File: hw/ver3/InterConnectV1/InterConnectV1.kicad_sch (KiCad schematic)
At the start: 3 parts, among them J1 Conn_02x04_Odd_Even, J3 RJ45, U5 SP3485EN

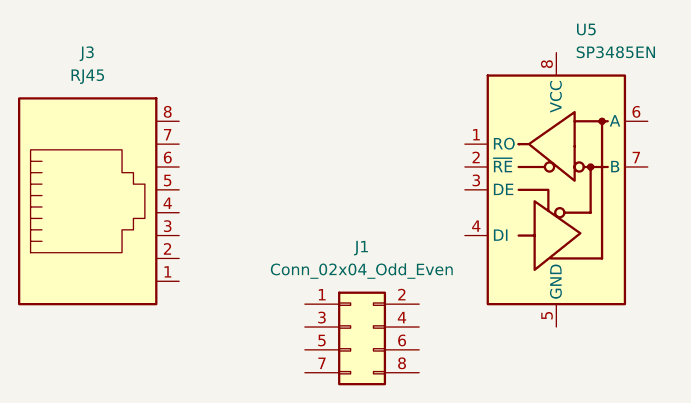
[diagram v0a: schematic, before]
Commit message: Redo some charger routing. Improve design for interconnect
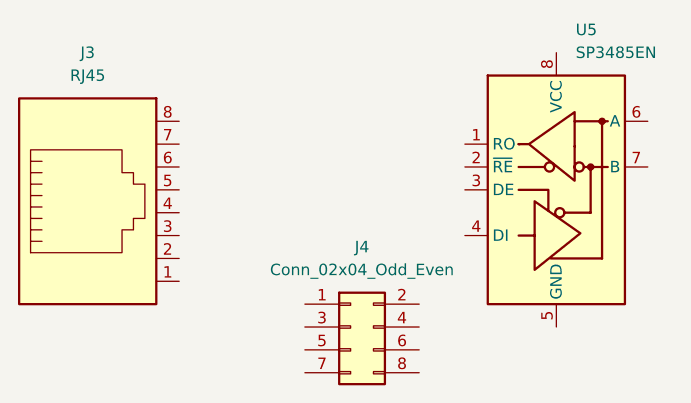
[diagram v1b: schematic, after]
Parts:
- renumbered J1 to J4
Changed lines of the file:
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@@
 		(dnp no)
 		(fields_autoplaced yes)
-		(property "Reference" "J1"
+		(property "Reference" "J4"
 			(at 125.73 93.98 0)
 			(effects
@@
 		)
 		(instances
+			(project "ChargerV3"
+				(path "/93408532-1ffa-463d-873c-16289d2b7987/f8cdf9d7-add1-4ff8-8430-918a71e3d1f9/aa801e4b-edfe-4a01-9e20-8e9249af9b44"
+					(reference "J4")
+					(unit 1)
+				)
+			)
 			(project ""
 				(path "/93a5de3b-2dc1-4e4f-9e25-5e90260a5115"
@@
 		)
 		(instances
+			(project "ChargerV3"
+				(path "/93408532-1ffa-463d-873c-16289d2b7987/f8cdf9d7-add1-4ff8-8430-918a71e3d1f9/aa801e4b-edfe-4a01-9e20-8e9249af9b44"
+					(reference "J3")
+					(unit 1)
+				)
+			)
 			(project "InterConnectV1"
 				(path "/93a5de3b-2dc1-4e4f-9e25-5e90260a5115"
@@
 		)
 		(instances
+			(project "ChargerV3"
+				(path "/93408532-1ffa-463d-873c-16289d2b7987/f8cdf9d7-add1-4ff8-8430-918a71e3d1f9/aa801e4b-edfe-4a01-9e20-8e9249af9b44"
+					(reference "U5")
+					(unit 1)
+				)
+			)
 			(project "InterConnectV1"
 				(path "/93a5de3b-2dc1-4e4f-9e25-5e90260a5115"

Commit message: Initial schematic for InterConnectV1
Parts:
- added C901, C905, C907: 10uF, Capacitor_SMD:C_0603_1608Metric, symbol Device:C
- added C902, C903, C904: 100nF, Capacitor_SMD:C_0603_1608Metric, symbol Device:C
- added C906, C908: 100uF-16v, Capacitor_SMD:CP_Elec_6.3x5.4, symbol Device:C_Polarized
- added D901: ACTIVITY, LED_SMD:LED_0805_2012Metric, symbol Device:LED
- added D902: PGOOD, LED_SMD:LED_0805_2012Metric, symbol Device:LED
- added D903: STPS360AF, Diode_SMD:D_SOD-128, symbol Device:D_Schottky
- added J902: TermEnable, Connector_PinHeader_2.54mm:PinHeader_1x02_P2.54mm_Vertical, symbol Connector:Conn_01x02_Pin
- added L901: 15uH, Inductor_SMD:L_12x12mm_H4.5mm, symbol Device:L_Ferrite
- added Q901: 2N7002, Package_TO_SOT_SMD:SOT-23, symbol Transistor_FET:2N7002
- added R901, R903: 47k, Resistor_SMD:R_0603_1608Metric, symbol Device:R_US
- added R902, R905, R906, R907, R908, R910: 10k, Resistor_SMD:R_0603_1608Metric, symbol Device:R_US
- added R904: 120, Resistor_SMD:R_0603_1608Metric, symbol Device:R_US
- added R909: 88.7k, Resistor_SMD:R_0603_1608Metric, symbol Device:R_US
- added U901: ST1S14PHR, Package_SO:TI_SO-PowerPAD-8, symbol Regulator_Switching:ST1S14PHR
- added U903: AMS1117-3.3, Package_TO_SOT_SMD:SOT-223-3_TabPin2, symbol Regulator_Linear:AMS1117-3.3
- added U904: AMS1117-5.0, Package_TO_SOT_SMD:SOT-223-3_TabPin2, symbol Regulator_Linear:AMS1117-5.0
- J901: renamed from J3; footprint (none) -> Connector_RJ:RJ45_Amphenol_54602-x08_Horizontal; Digikey (none) -> 609-1046-ND; LCSC (none) -> C2847314
- J903: renamed from J4; value Conn_02x04_Odd_Even -> DataBusSelector; Digikey (none) -> PH2-08-UA; LCSC (none) -> C492421
- U902: renamed from U5; Digikey (none) -> 4518-SP3485EENTR-ND; LCSC (none) -> C668205
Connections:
- net IO_DATA_A1: now reaches J903.1 (Pin_1)
- net IO_DATA_A1: now also J901.1
- net at J903.2 (Pin_2): now also J903.4 (Pin_4), U902.6 (A), J902.1 (Pin_1)
- net IO_DATA_A2: now reaches J903.3 (Pin_3)
- net IO_DATA_A2: now also J901.3
- net IO_DATA_B1: now reaches J903.5 (Pin_5)
- net IO_DATA_B1: now also J901.2
- net at J903.6 (Pin_6): now also J903.8 (Pin_8), U902.7 (B), R904.1
- net IO_DATA_B2: now reaches J903.7 (Pin_7)
- net IO_DATA_B2: now also J901.6
- net IO_PWR_+48V: now reaches J901.4
- net IO_PWR_+48V: now also J901.5, C901.1, C902.1, R901.1, R903.1, U901.5 (EN2), U901.7 (VIN)
- net GND: now reaches J901.7
- net GND: now also J901.8, U902.5 (GND), C901.2, C902.2, C904.2, C905.2, C906.2, C907.2, C908.2, D903.2 (A), Q901.2 (S), R902.1, R905.1, R906.1, R907.1, R908.1, R910.1, U901.3 (~{EN1}), U901.6 (GND), U901.9 (PADGND), U903.1 (GND), U904.1 (GND)
- net IC_DATA_OUT: now reaches U902.1 (RO)
- net IC_DATA_OUT: now also R907.2
- net IC_RTX_EN: now reaches U902.2 (~{RE})
- net IC_RTX_EN: now also U902.3 (DE), R906.2
- net IC_DATA_IN: now reaches U902.4 (DI)
- net IC_DATA_IN: now also R905.2
- net +3V3: now reaches U902.8 (VCC)
- net +3V3: now also C904.1
- new net: C903.1, D903.1 (K), L901.2, U901.8 (SW)
- new net: D901.2 (A), R901.2
- new net: D902.1 (K), U901.2 (PG)
- new net: D902.2 (A), R903.2
- new net: R908.2, R909.2, U901.4 (FB)
- new net: C903.2, U901.1 (BOOT)
- new net: J902.2 (Pin_2), R904.2
- new net: D901.1 (K), Q901.3 (D)
- new net IC_ACTIVITY_LED_DRIVE: Q901.1 (G), R902.2
- new net IC_PWR_12V: C906.1, C908.1, L901.1, R909.1, R910.2, U904.3 (VI)
- new net IC_PWR_3V3: C907.1, U903.2 (VO)
- new net IC_PWR_5V: C905.1, U903.3 (VI), U904.2 (VO)
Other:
- note added: "DC-DC Converter: 15V-48V IN, 12V 3A OUT"
- note added: "Data Activity LED Driver"
- note added: "Inductor P/N & pad sized to fit multiple components"
- note added: "Needs jumpers/shunts: - Digikey: QPC02SXGN-RC - LCSC: C100114"
- note added: "RJ45 IO Connector"
- note added: "RS485 Half-Duplex Transciever"
- moved on the sheet: J901, J903, U902

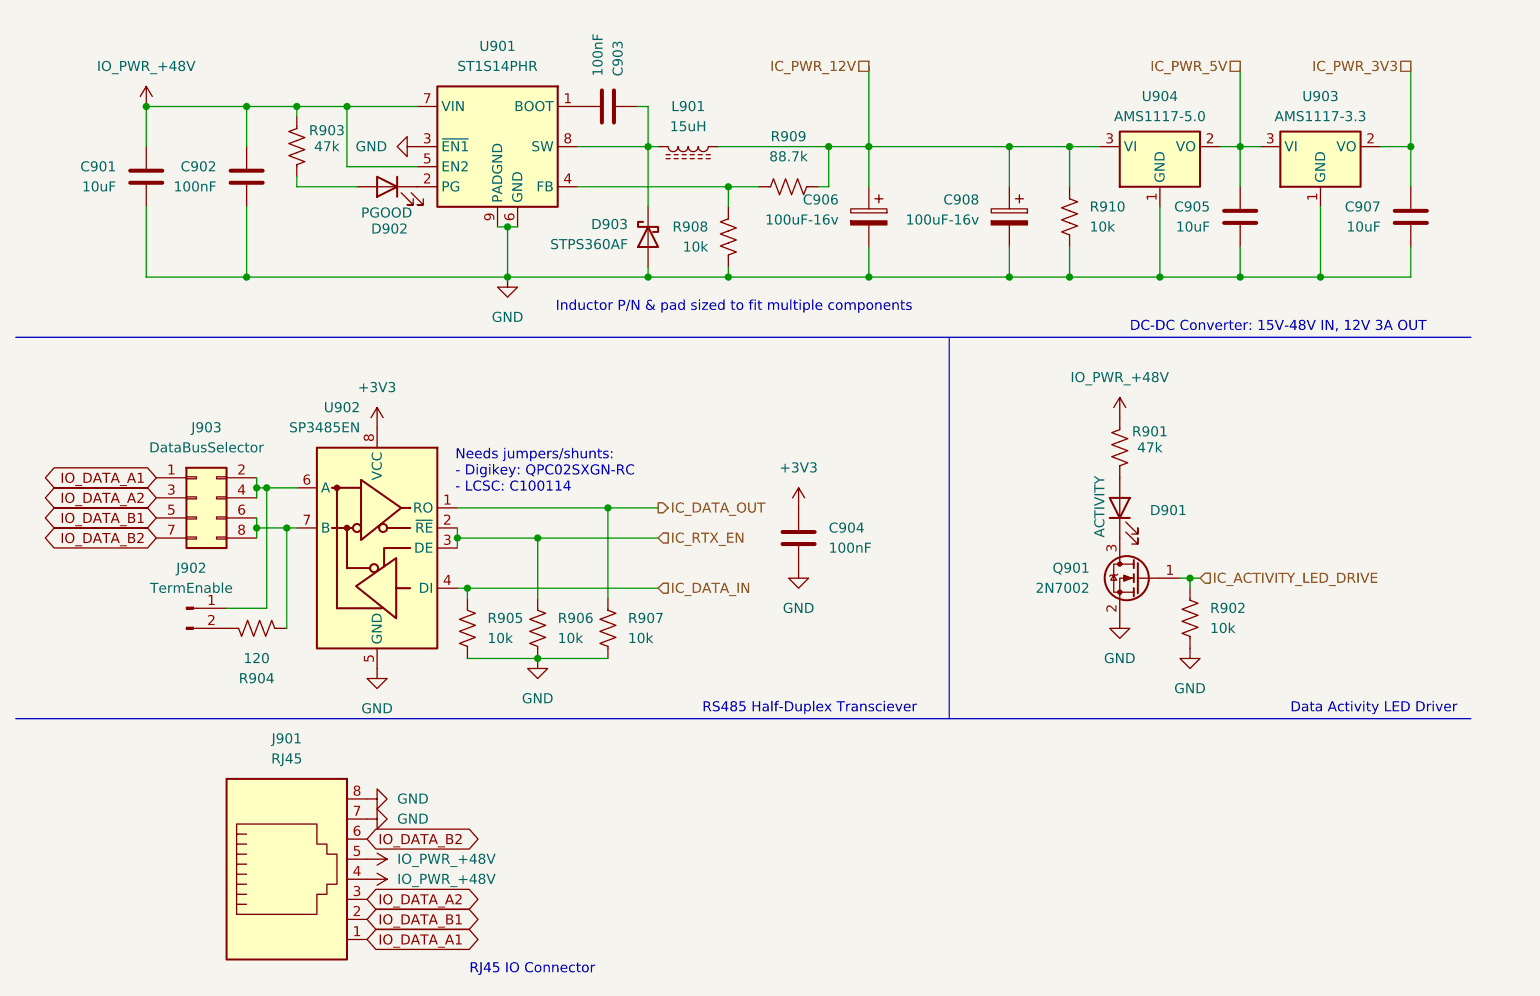
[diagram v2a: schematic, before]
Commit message: Nearly final charger schematic, updated with RS485 interconnect.
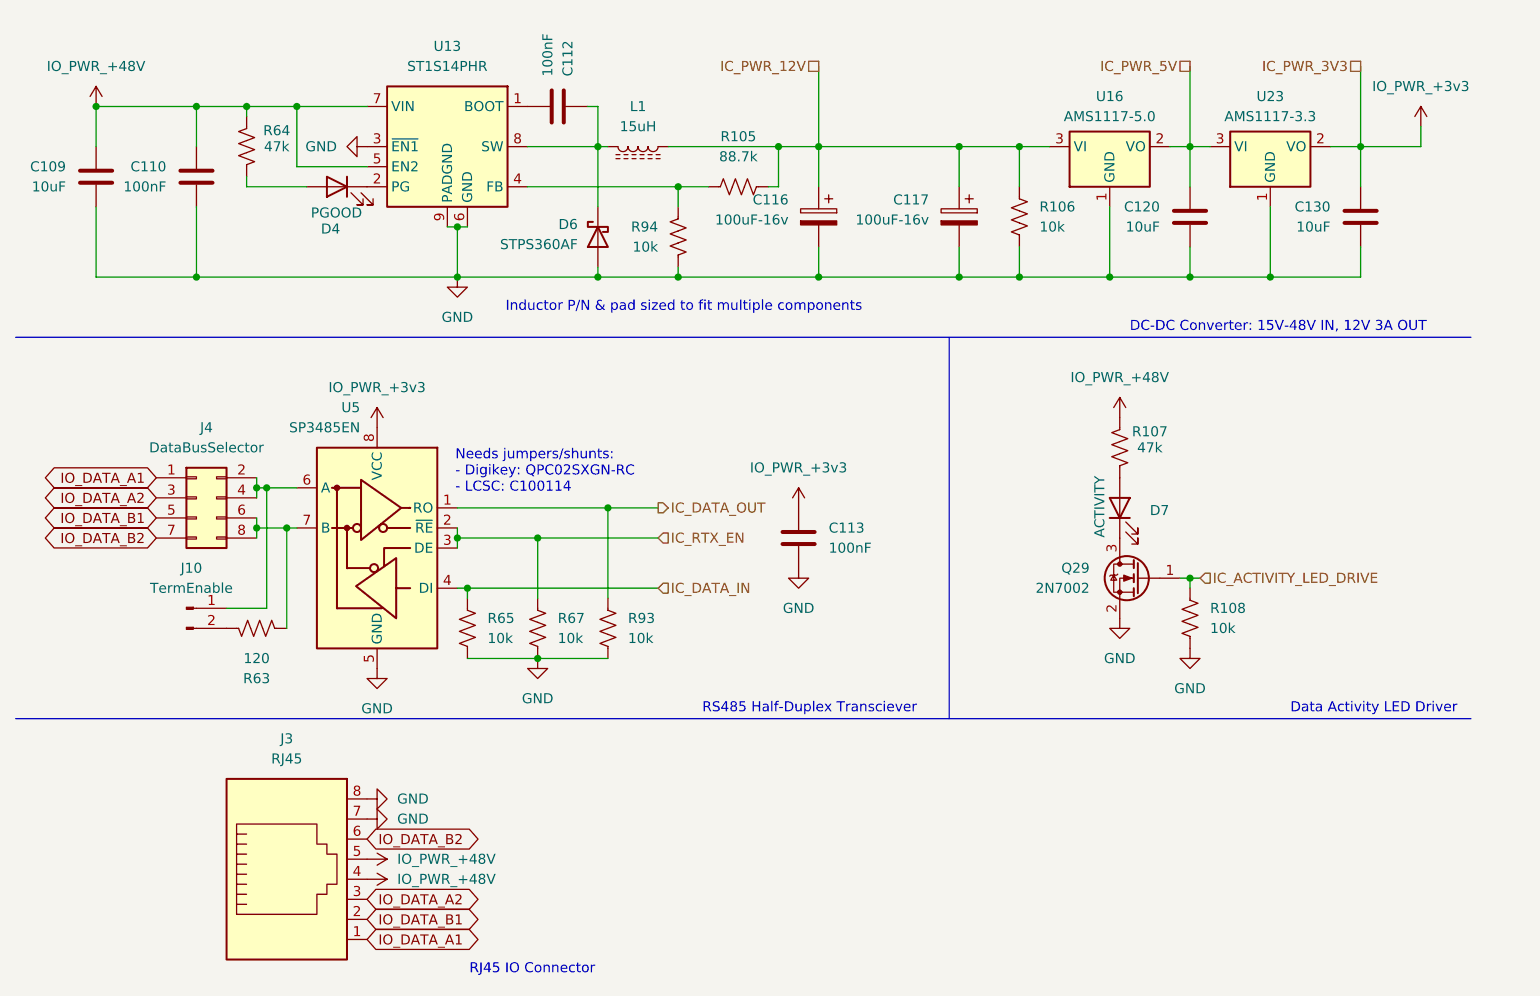
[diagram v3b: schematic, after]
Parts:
- removed C904: 100nF, Capacitor_SMD:C_0603_1608Metric, symbol Device:C
- removed C905: 10uF, Capacitor_SMD:C_0603_1608Metric, symbol Device:C
- removed D902: PGOOD, LED_SMD:LED_0805_2012Metric, symbol Device:LED
- added C113: 100nF, Capacitor_SMD:C_0603_1608Metric, symbol Device:C
- added C120: 10uF, Capacitor_SMD:C_0603_1608Metric, symbol Device:C
- added D4: PGOOD, LED_SMD:LED_0805_2012Metric, symbol Device:LED
- renumbered C901 to C109, C902 to C110, C903 to C112, C906 to C116, C908 to C117, C907 to C130, D903 to D6, D901 to D7, J902 to J10, J901 to J3, J903 to J4, L901 to L1, Q901 to Q29, R909 to R105, R910 to R106, R901 to R107, R902 to R108, R904 to R63, R903 to R64, R905 to R65, R906 to R67, R907 to R93, R908 to R94, U901 to U13, U904 to U16, U903 to U23, U902 to U5
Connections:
- net IC_PWR_3V3 is gone; now on net IO_PWR_+3v3: C130.1, U23.2 (VO)
- net GND: now also C113.2, C120.2
- net IC_PWR_5V: now also C120.1
- net at U13.2 (PG): now also D4.1 (K)
- net at R64.2: now also D4.2 (A)
- net +3V3 renamed IO_PWR_+3v3
- net IO_PWR_+3v3: now also C113.1
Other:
- moved on the sheet: C109, C110, C112, C116, C117, C130, D6, L1, R105, R106, R64, R94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

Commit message: Sync board changes from before work started
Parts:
- removed D7: ACTIVITY, LED_SMD:LED_0805_2012Metric, symbol Device:LED
- removed J3: RJ45, Connector_RJ:RJ45_Amphenol_54602-x08_Horizontal, symbol Connector:RJ45
- removed Q29: 2N7002, Package_TO_SOT_SMD:SOT-23, symbol Transistor_FET:2N7002
- removed R107: 47k, Resistor_SMD:R_0603_1608Metric, symbol Device:R_US
- removed R108: 10k, Resistor_SMD:R_0603_1608Metric, symbol Device:R_US
- added J3: DataIN, Connector_RJ:RJ45_Amphenol_RJHSE538X, symbol Connector:RJ45_LED_Shielded
- added J6: DataOUT, Connector_RJ:RJ45_Amphenol_RJHSE538X, symbol Connector:RJ45_LED_Shielded
- added R25, R5, R58, R59: 3k, Resistor_SMD:R_0603_1608Metric, symbol Device:R_US
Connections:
- net GND: now also J3.7, J3.8, J3.SH, J6.7, J6.8, J6.SH
- net IO_DATA_A1: now also J3.1, J6.1
- net IO_DATA_A2: now also J3.3, J6.3
- net IO_DATA_B1: now also J3.2, J6.2
- net IO_DATA_B2: now also J3.6, J6.6
- net IO_PWR_+48V: now also J3.4, J3.5, J6.4, J6.5
- net IC_PWR_5V renamed IO_PWR_+5V
- net IO_PWR_+5V: now also R25.2, R5.2, R58.2, R59.2
- new net: J3.10, R5.1
- new net: J6.12, R59.1
- new net: J3.12, R25.1
- new net: J6.10, R58.1
- new net IC_LED_IN_G: J3.9
- new net IC_LED_IN_Y: J3.11
- new net IC_LED_OUT_G: J6.9
- new net IC_LED_OUT_Y: J6.11
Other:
- note added: "This schematic is intended for a single node in the system. It supplies power, a selectable RS485 channel, and two IO ports to allow for extending the network to more nodes."
- note removed: "Data Activity LED Driver"
- moved on the sheet: C113, J10, J4, R63, R65, R67, R93, U5
